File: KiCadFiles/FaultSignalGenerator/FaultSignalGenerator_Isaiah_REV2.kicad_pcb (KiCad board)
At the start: 2 copper layers, 17 parts, among them J1 Conn_02x20_Counter_Clockwise, U1 TL074CDR, U2 MCP4462-502E/ST, U3 PCM1681PWP

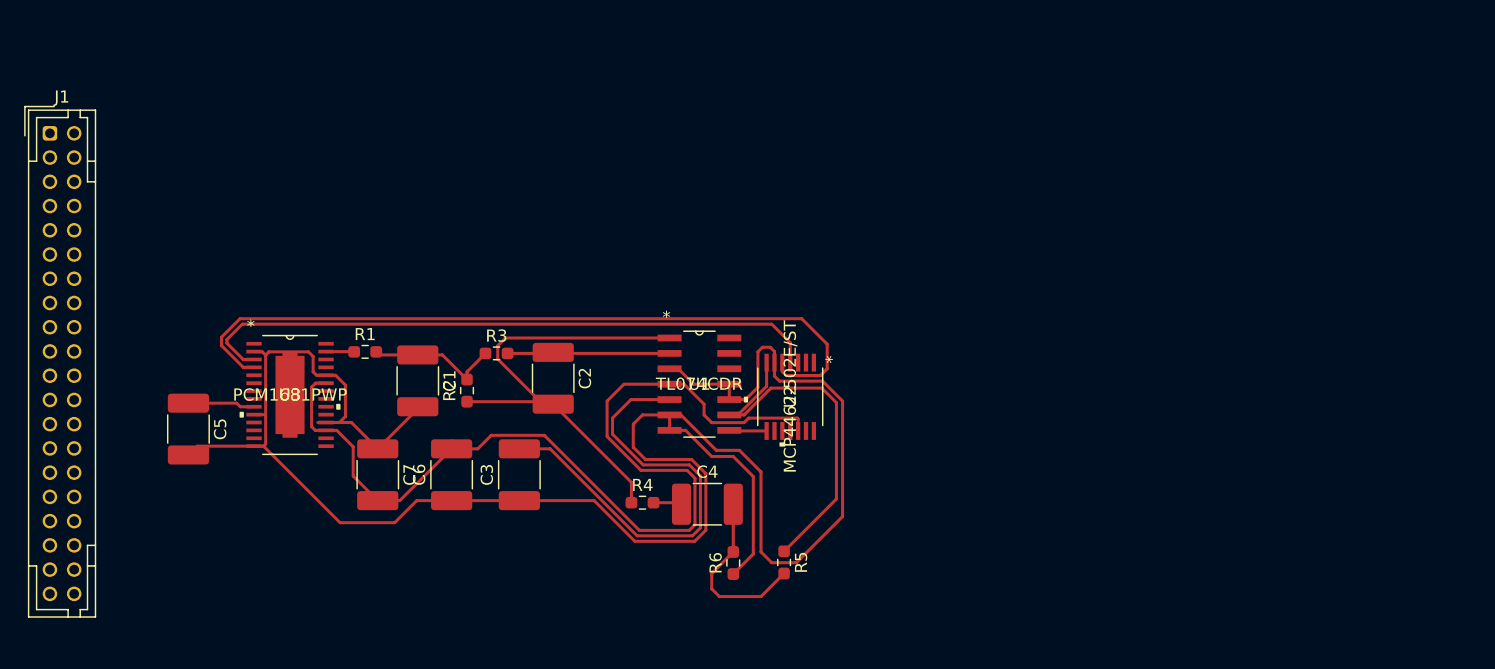
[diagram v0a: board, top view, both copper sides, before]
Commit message: Partial Single Channel PCB
Just wrapped this up this morning. Includes all of the current parts in the schematic. Once a voltage regulator and linear regulator are selected I'll include those as well. Just one layer currently.
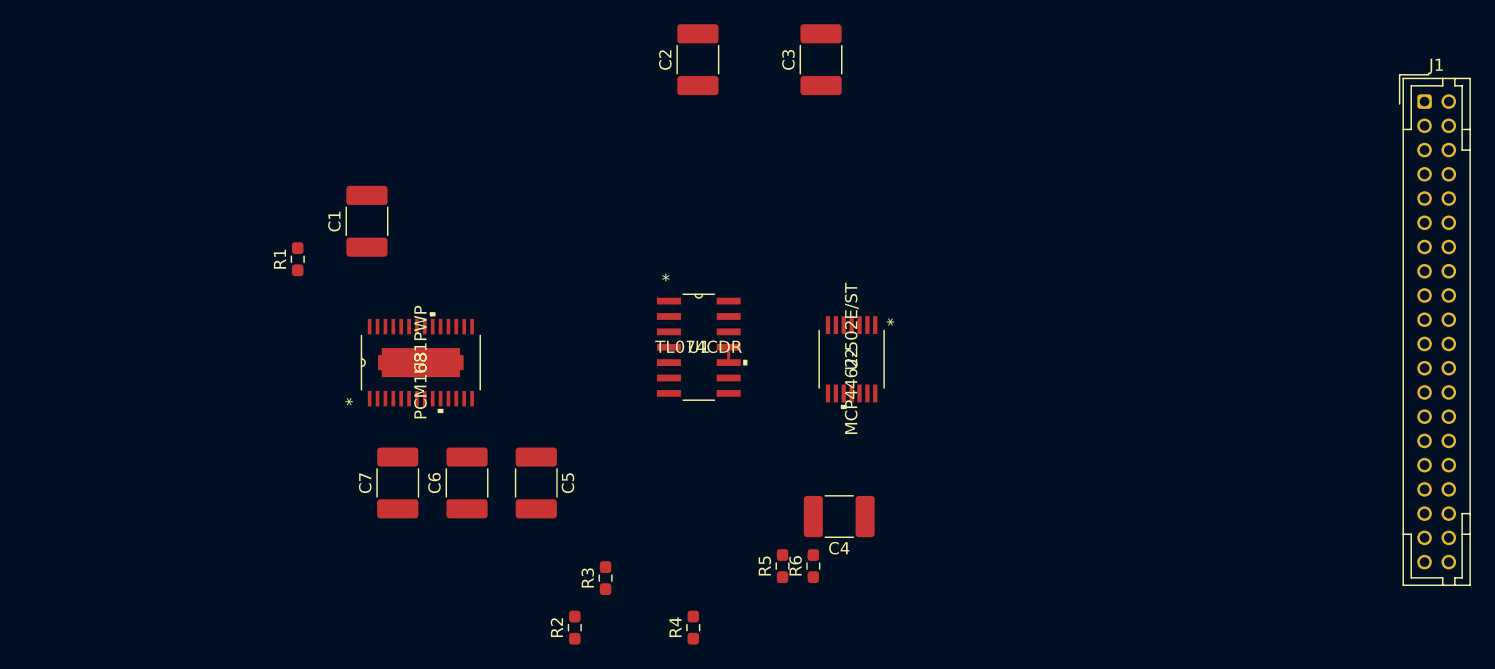
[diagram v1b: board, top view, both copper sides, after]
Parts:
- moved J1 113.5 mm to (161.6, 64.8)
- moved C3 42.3 mm to (111.8, 61.4)
- moved C5 29.0 mm to (88.3, 96.3)
- moved C2 28.9 mm to (101.6, 61.4), turned to 90 degrees
- moved R2 21.5 mm to (91.4, 108.2)
- moved R3 20.6 mm to (94.0, 104.1), turned to 90 degrees
- moved C1 13.8 mm to (74.3, 74.7), turned to 90 degrees
- moved R4 11.1 mm to (101.2, 108.2), turned to 90 degrees
- moved U3 11.1 mm to (78.7, 86.4), turned to 90 degrees
- moved C4 10.9 mm to (113.3, 99.1), turned to 180 degrees
- moved R1 9.45 mm to (68.6, 77.8), turned to 90 degrees
- moved R6 6.61 mm to (111.1, 103.1)
- moved U2 5.94 mm to (114.3, 86.1)
- moved U1 3.05 mm to (101.7, 85.1)
- moved C7 1.78 mm to (76.8, 96.3), turned to 90 degrees
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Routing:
- net 0: track 172.5 -> 1.27 mm
- net +1V5: track 81.3 -> 0.00 mm
- net SDA: track 62.4 -> 0.00 mm
- net SCL: track 52.4 -> 0.00 mm
- net Net-(C2-Pad2): track 39.7 -> 0.00 mm
- net Net-(C3-Pad2): track 37.8 -> 0.00 mm
- net Net-(R5-Pad1): track 30.3 -> 0.00 mm
- net out: track 14.7 -> 0.00 mm
- net Net-(C2-Pad1): track 13.4 -> 0.00 mm
- net Net-(C1-Pad1): track 11.2 -> 0.00 mm
- net +3.3V: track 5.53 -> 0.00 mm
- net Net-(U1-Pad8): track 3.10 -> 0.00 mm
- net Net-(C4-Pad1): track 2.36 -> 0.00 mm
- net DAC: track 2.32 -> 0.00 mm
